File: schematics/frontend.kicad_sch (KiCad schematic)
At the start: 28 parts

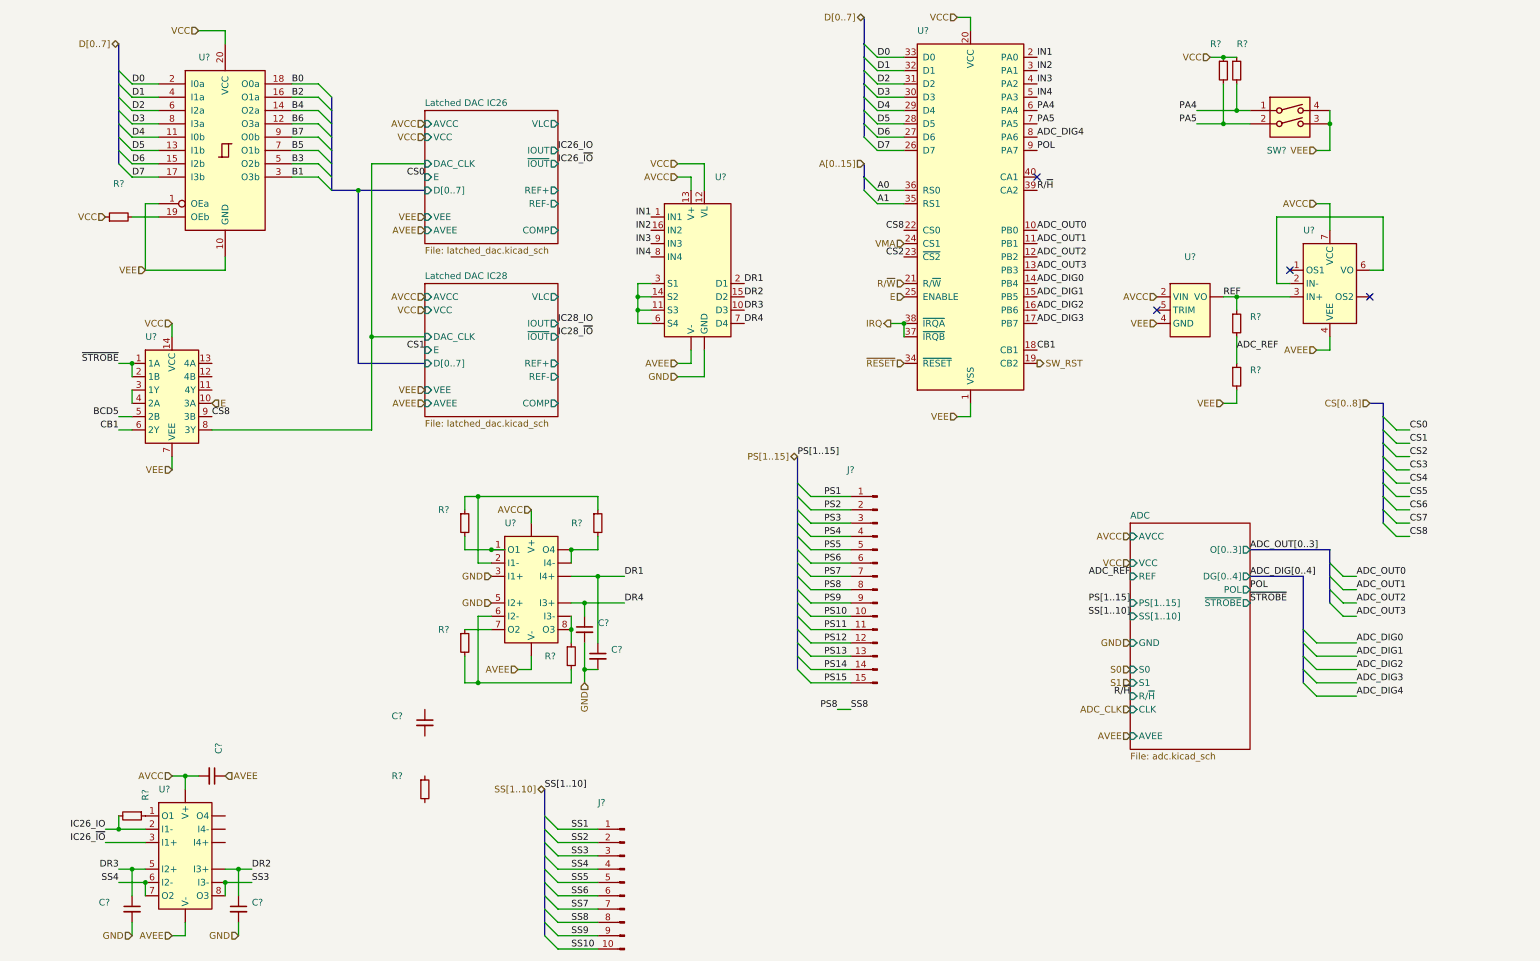
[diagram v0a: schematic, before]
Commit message: Moved more components into hierachical sheets, misc cleanup
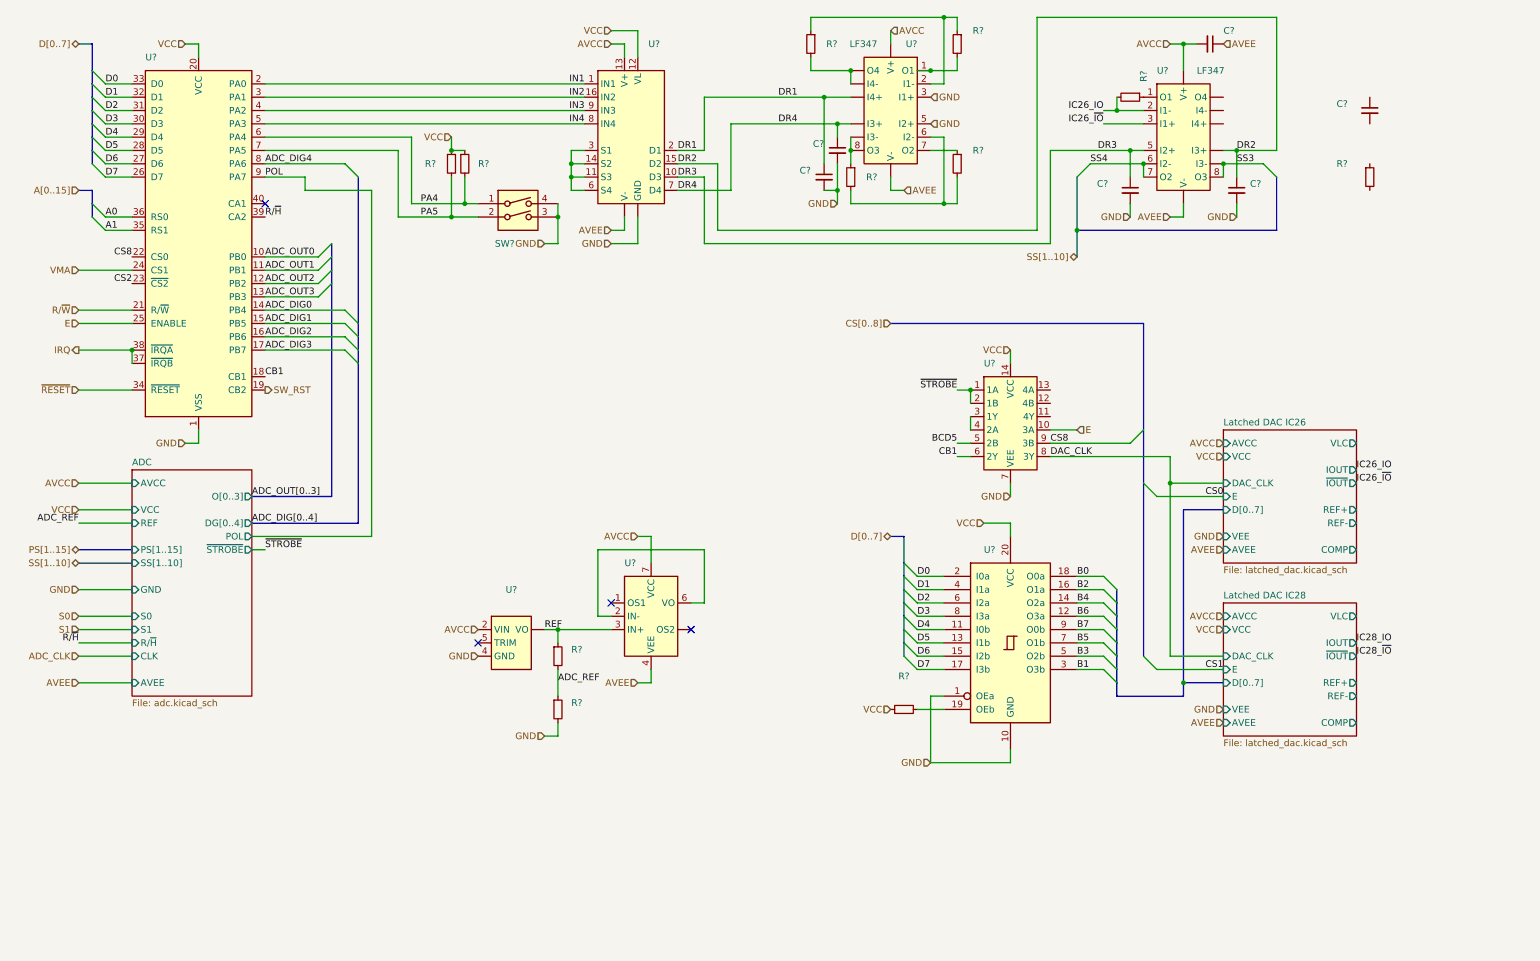
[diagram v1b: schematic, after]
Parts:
- removed J?: ~, symbol Connector:Conn_01x15_Male
- removed J?: ~, symbol Connector:Conn_01x10_Male
- U? (x2): value ~ -> LF347
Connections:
- net SS3 is gone; now on net DR2: U?. (V-), U?.8 (O3)
- net VEE is gone; now on net GND: R?.2, SW?.3, SW?.4, U?.1 (OEa), U?.1 (VSS), U?.10 (GND), U?.4 (GND), U?.7 (VEE)
- net Latched DAC IC26/DAC_CLK renamed DAC_CLK
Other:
- moved on the sheet: C?, R?, SW?, U?

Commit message: cleanup, fixes, started on power supplies
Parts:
- removed R? (x2): ~, symbol Device:R_Small
- removed U?: ~, symbol Custom:LT1021
- removed U?: ~, symbol Custom:LF411
- added C21, C23, C44, C52, C56, C58: 100n, symbol Device:C_Small
- added IC31: LF411, symbol Custom:LF411
- added IC32: LT1021, symbol Custom:LT1021
- added R30, R?: 5k11, symbol Device:R_Small
- C51, C52, C54, C59: renamed from C?; value ~ -> 220n
- C67: renamed from C?; value ~ -> 100p
- IC18: renamed from U?; footprint (none) -> Package_DIP:DIP-40_W15.24mm
- IC21: renamed from U?; value ~ -> 74LS00
- IC25: renamed from U?; value ~ -> 74LS241
- IC33: renamed from U?; value ~ -> DG211
- R21, R22, R41, R42, R45, R46: renamed from R?; value ~ -> 10k
- R49: renamed from R?; value ~ -> 21R
- R50: renamed from R?; value ~ -> 3k48
- gave numbers to parts that had none: 4
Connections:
- net AVCC: now also C21.1, C58.1, IC31.7 (VCC), IC32.2 (VIN)
- net AVEE: now also C52.2, C56.2, IC31.4 (VEE); no longer C57.1
- net GND: now also C57.1, C21.2, C23.1, C44.1, C52.1, C56.1, C58.2, IC32.4 (GND)
- net IC28_IO: now also C67.1, IC36. (V-), R50.2
- net Latched DAC IC26/REF+: now also R?.1
- net Latched DAC IC28/REF+: now also R30.1
- net REF: now also IC31.3 (IN+), IC32. (VO)
- net VCC: now also C23.2, C44.2
- net at C67.2: now also IC33.11 (S3), IC33.14 (S2), IC33.3 (S1), IC33.6 (S4), R50.1
- net PS4: now reaches IC35.1 (O1), R45.2
- net PS3: now reaches IC35.7 (O2), R41.1
- net IC26_~{IO} renamed ~{IC26_IO}
- new net DAC_REF: IC31.2 (IN-), IC31.6 (VO), R30.2, R?.2
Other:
- moved on the sheet: C54, C57, C59, C67, IC21, IC25, IC36, R21, R22, R41, R49, R50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

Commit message: More power supply work
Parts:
- removed R30, R?: 5k11, symbol Device:R_Small
- IC21: value 74LS00 -> 74LD00
- IC25: value 74LS241 -> 74LD241
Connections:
- net BCD5 is gone; now on net ADC_S4: IC21.5 (2B)
- net AVCC: now also IC35.4 (V+), IC36.4 (V+); no longer IC31.7 (VCC), IC35. (V-), IC36. (V-)
- net AVEE: now also IC31.8 (VOS), IC35.11 (V-), IC36.11 (V-); no longer IC31.4 (VEE), IC35. (V-), IC36. (V-)
- net DAC_REF: now also IC31.3 (+); no longer IC31.2 (IN-), IC31.6 (VO)
- net DR1: now also IC35.12 (I4+); no longer IC35. (V-)
- net DR2: now also IC36.10 (I3+); no longer IC36. (V-), IC36.8 (O3)
- net DR4: now also IC35.10 (I3+); no longer IC35. (V-)
- net IC28_IO: now also IC36.13 (I4-); no longer IC36. (V-)
- net REF: no longer IC31.3 (IN+)
- net at R46.2: now also IC35.13 (I4-), IC35.14 (O4); no longer IC35. (V-)
- net at IC35.8 (O3), R42.1: now also IC35.9 (I3-); no longer IC35. (V-)
- net ADC_DIG0 renamed ADC_S0
- net ADC_DIG1 renamed ADC_S1
- net ADC_DIG2 renamed ADC_S2
- net ADC_DIG3 renamed ADC_S3
- net ADC_DIG4 renamed ADC_S4
- new net SS3: IC36.8 (O3), IC36.9 (I3-)
- no-connect marks 4 -> 2
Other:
- sheet Latched DAC IC26 ports: added GND; removed COMP, VEE, VLC
- sheet Latched DAC IC28 ports: added GND; removed COMP, VEE, VLC
- note added: "DR1 is PS VREF"
- note added: "SW3 selects between 25V 2A and 50V 1A modes"
- moved on the sheet: C54, C57, C59, C67, IC21, IC25, IC31, R49, R50, R?

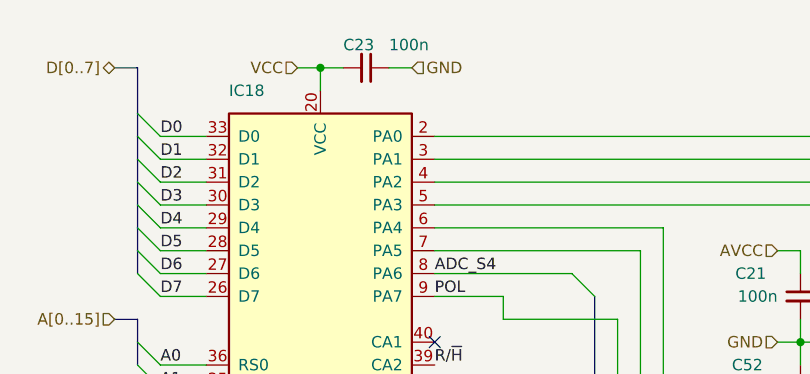
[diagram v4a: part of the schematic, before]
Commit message: Updated to KiCad v10.0. Minor improvements.
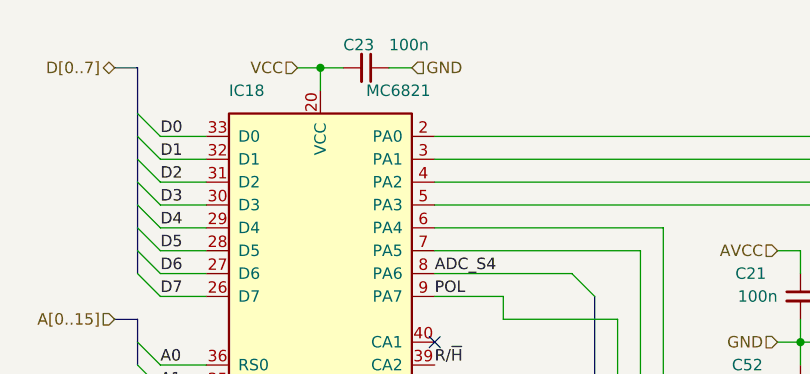
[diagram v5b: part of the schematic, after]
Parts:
- C57, R?, SW3: value ~ -> (none)
- IC18: value ~ -> MC6821
